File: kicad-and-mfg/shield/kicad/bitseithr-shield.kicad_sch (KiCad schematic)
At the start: 59 parts, among them CN1 SHIELD CONN 2, CN10 SHIELD CONN 3, CN11 SHIELD CONN 4, CN12 SHIELD CONN 5, CN2 SHIELD CONN 7, CN3 SHIELD CONN 8, CN9 SHIELD CONN 6, IC1 AY-3-8912_28PIN, IC2 AY-3-8912_28PIN, J10 Communication, J11 OLED Connector, J4 Power, J5 Analog, J6 Analog, J7 Digital, J8 PWM, J9 PWM, P1 SHIELD CONN 1, U1 OPA1692

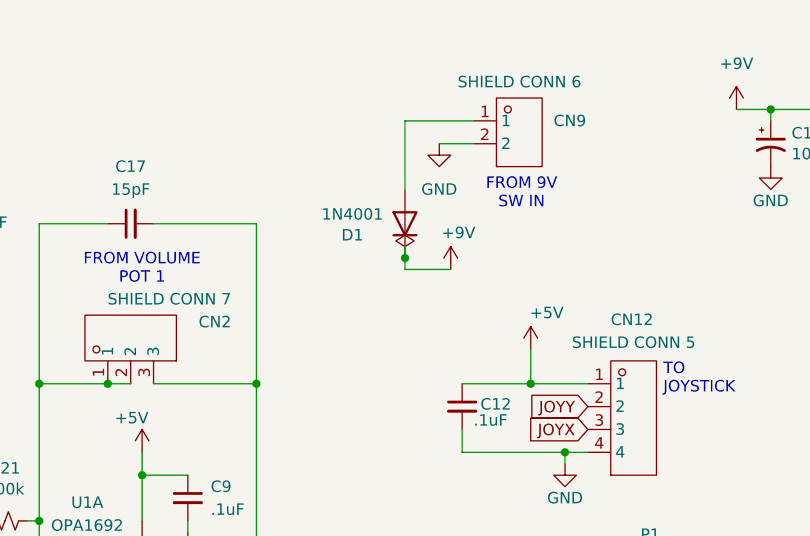
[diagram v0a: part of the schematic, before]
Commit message: added lcsc part nos to shield schematic
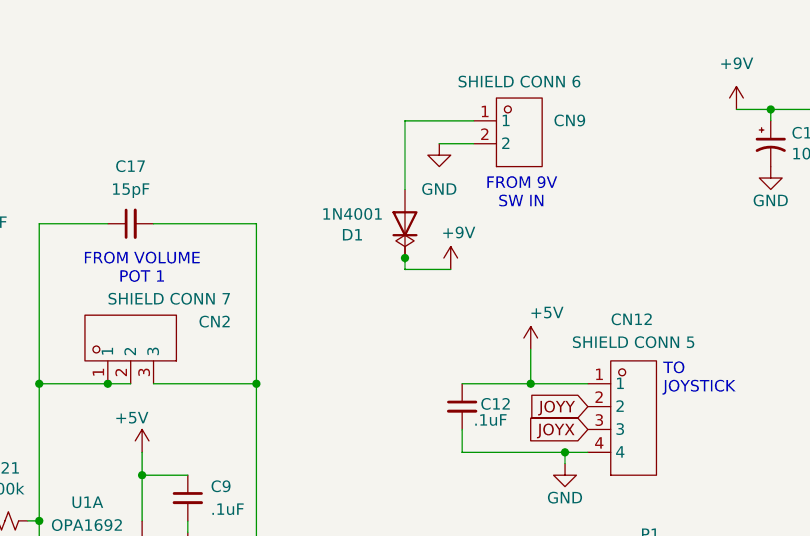
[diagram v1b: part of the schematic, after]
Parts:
- C1, C12, C14, C3, C7, C8, C9: footprint (none) -> Capacitor_SMD:C_0805_2012Metric; LCSC (none) -> C49678
- C10, C11: footprint Capacitor_THT:CP_Radial_D6.3mm_P2.50mm -> Capacitor_THT:CP_Radial_D8.0mm_P3.50mm; LCSC (none) -> C116228
- C13, C5, C6: footprint Capacitor_THT:CP_Radial_D5.0mm_P2.50mm -> Capacitor_SMD:C_1206_3216Metric; LCSC (none) -> C13585
- C15: footprint Capacitor_THT:CP_Radial_D5.0mm_P2.50mm -> Capacitor_THT:CP_Radial_D5.0mm_P2.00mm; LCSC (none) -> C88726
- C16, C17: footprint Capacitor_SMD:C_0603_1608Metric_Pad1.08x0.95mm_HandSolder -> Capacitor_SMD:C_0603_1608Metric; LCSC C106997 -> C1644
- C18, C19, C20, C21, C22, C23: footprint (none) -> Capacitor_THT:C_Rect_L7.2mm_W5.0mm_P5.00mm
- CN1: LCSC (none) -> C2845813; LCSC Part Name 1x8P 间距:2.5mm 弯插 系列:XA -> (none); Manufacturer HCTL(华灿天禄) -> (none); Manufacturer Part HC-XA-8AW -> (none); Supplier LCSC -> (none); Supplier Part C2845813 -> (none)
- CN10, CN11, CN9: LCSC (none) -> C2845807; LCSC Part Name 1x2P 间距:2.5mm 弯插 系列:XA -> (none); Manufacturer HCTL(华灿天禄) -> (none); Manufacturer Part HC-XA-2AW -> (none); Supplier LCSC -> (none); Supplier Part C2845807 -> (none)
- CN12: LCSC (none) -> C2845809; LCSC Part Name 1x4P 间距:2.5mm 弯插 系列:XA -> (none); Manufacturer HCTL(华灿天禄) -> (none); Manufacturer Part HC-XA-4AW -> (none); Supplier LCSC -> (none); Supplier Part C2845809 -> (none)
- CN2, CN3: LCSC (none) -> C2845808; LCSC Part Name 1x3P 间距:2.5mm 弯插 系列:XA -> (none); Manufacturer HCTL(华灿天禄) -> (none); Manufacturer Part HC-XA-3AW -> (none); Supplier LCSC -> (none); Supplier Part C2845808 -> (none)
- D1: footprint Diode_SMD:D_SMA_Handsoldering -> Diode_SMD:D_SMA; LCSC (none) -> C2909965
- J11: LCSC (none) -> C160404
- P1: LCSC (none) -> C9144; LCSC Part Name 2.54mm 2x10P 排数:2 每排P数:10 -> (none); Manufacturer BOOMELE(博穆精密) -> (none); Manufacturer Part 2.54-2*10P弯简牛 -> (none); Supplier LCSC -> (none); Supplier Part C9144 -> (none)
- R11, R18, R20, R6, R7, R8: footprint (none) -> Resistor_SMD:R_0603_1608Metric; LCSC (none) -> C110776
- R12, R13, R14, R15, R16, R17, R19, R21: LCSC (none) -> C2073484
- U1: LCSC (none) -> C2060550; LCSC Part Name 低功耗、低噪声和低失真音频运算放大器 -> (none); Manufacturer TI(德州仪器) -> (none); Manufacturer Part OPA1692IDR -> (none); Supplier LCSC -> (none); Supplier Part C2060550 -> (none)
